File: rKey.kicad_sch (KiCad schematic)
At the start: 38 parts, among them IC1 BDX34C, J1 Conn_01x06, Q1 BC337, Q2 BC337, Q3 BC337, Q4 BC337, Q5 BC327, Q8 BC337, U1 TL084BCN, U2 LM7810_TO220

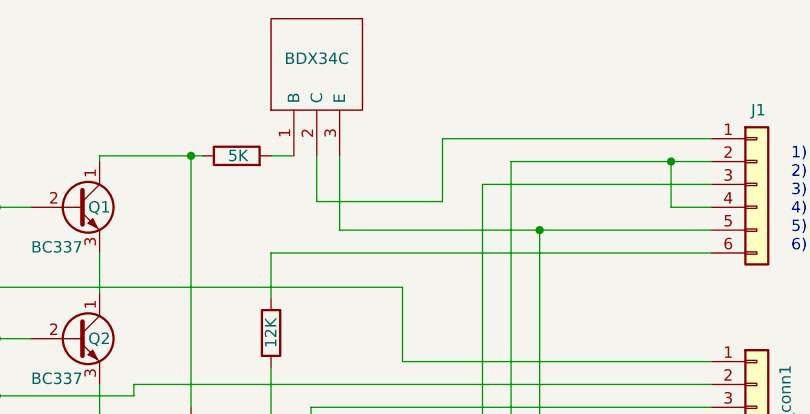
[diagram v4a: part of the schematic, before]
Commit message: Fix: floating tranistor's base
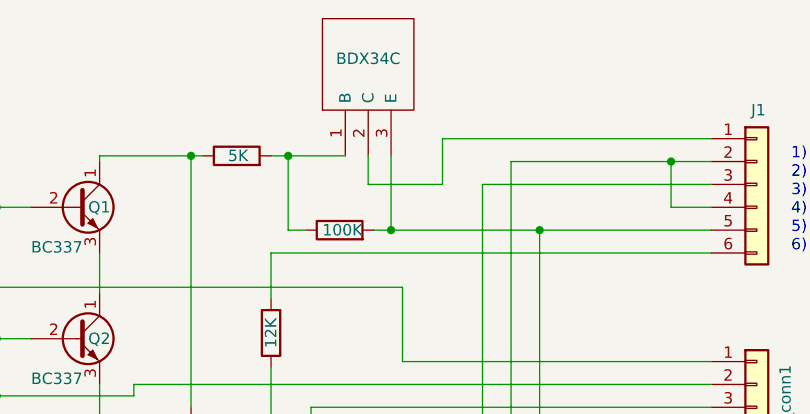
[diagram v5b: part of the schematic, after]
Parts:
- added R11: 100K, Resistor_THT:R_Axial_DIN0207_L6.3mm_D2.5mm_P10.16mm_Horizontal, symbol Device:R
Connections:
- net at IC1.1 (B), R10.2: now also R11.1
- net at IC1.3 (E), J1.5 (Pin_5), R6.2: now also R11.2
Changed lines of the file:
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@@
   (junction (at 200.025 86.36) (diameter 0) (color 0 0 0 0)
   )
+  (junction (at 201.93 53.34) (diameter 0) (color 0 0 0 0)
+  )
   (junction (at 76.2 92.71) (diameter 0) (color 0 0 0 0)
   )
@@
   )
   (junction (at 77.47 76.835) (diameter 0) (color 0 0 0 0)
+  )
+  (junction (at 213.36 61.595) (diameter 0) (color 0 0 0 0)
   )
   (junction (at 59.055 116.205) (diameter 0) (color 0 0 0 0)
@@
     (stroke (width 0) (type default) (color 0 0 0 0))
   )
+  (wire (pts (xy 201.93 61.595) (xy 201.93 53.34))
+    (stroke (width 0) (type default) (color 0 0 0 0))
+  )
   (wire (pts (xy 204.47 81.28) (xy 248.92 81.28))
     (stroke (width 0) (type default) (color 0 0 0 0))
@@
     (stroke (width 0) (type default) (color 0 0 0 0))
   )
-  (wire (pts (xy 219.075 58.42) (xy 219.075 51.435))
+  (wire (pts (xy 219.075 56.515) (xy 219.075 51.435))
     (stroke (width 0) (type default) (color 0 0 0 0))
   )
@@
     (stroke (width 0) (type default) (color 0 0 0 0))
   )
+  (wire (pts (xy 200.025 53.34) (xy 201.93 53.34))
+    (stroke (width 0) (type default) (color 0 0 0 0))
+  )
   (wire (pts (xy 149.86 59.055) (xy 157.48 59.055))
     (stroke (width 0) (type default) (color 0 0 0 0))
@@
     (stroke (width 0) (type default) (color 0 0 0 0))
   )
+  (wire (pts (xy 211.455 61.595) (xy 213.36 61.595))
+    (stroke (width 0) (type default) (color 0 0 0 0))
+  )
   (wire (pts (xy 138.43 87.63) (xy 138.43 95.25))
     (stroke (width 0) (type default) (color 0 0 0 0))
@@
     (stroke (width 0) (type default) (color 0 0 0 0))
   )
-  (wire (pts (xy 207.645 61.595) (xy 229.87 61.595))
+  (wire (pts (xy 213.36 61.595) (xy 229.87 61.595))
     (stroke (width 0) (type default) (color 0 0 0 0))
   )
@@
     (stroke (width 0) (type default) (color 0 0 0 0))
   )
-  (wire (pts (xy 205.105 53.34) (xy 205.105 58.42))
+  (wire (pts (xy 210.82 53.34) (xy 210.82 56.515))
     (stroke (width 0) (type default) (color 0 0 0 0))
   )
@@
     (stroke (width 0) (type default) (color 0 0 0 0))
   )
-  (wire (pts (xy 200.025 53.34) (xy 202.565 53.34))
-    (stroke (width 0) (type default) (color 0 0 0 0))
-  )
   (wire (pts (xy 167.64 100.965) (xy 167.64 95.25))
     (stroke (width 0) (type default) (color 0 0 0 0))
@@
     (stroke (width 0) (type default) (color 0 0 0 0))
   )
-  (wire (pts (xy 207.645 61.595) (xy 207.645 53.34))
+  (wire (pts (xy 213.36 61.595) (xy 213.36 53.34))
     (stroke (width 0) (type default) (color 0 0 0 0))
   )
@@
     (stroke (width 0) (type default) (color 0 0 0 0))
   )
-  (wire (pts (xy 205.105 58.42) (xy 219.075 58.42))
+  (wire (pts (xy 210.82 56.515) (xy 219.075 56.515))
     (stroke (width 0) (type default) (color 0 0 0 0))
   )
@@
     (stroke (width 0) (type default) (color 0 0 0 0))
   )
+  (wire (pts (xy 203.835 61.595) (xy 201.93 61.595))
+    (stroke (width 0) (type default) (color 0 0 0 0))
+  )
   (wire (pts (xy 47.625 81.28) (xy 47.625 76.2))
     (stroke (width 0) (type default) (color 0 0 0 0))
@@
   )
   (wire (pts (xy 89.535 95.25) (xy 93.98 95.25))
+    (stroke (width 0) (type default) (color 0 0 0 0))
+  )
+  (wire (pts (xy 201.93 53.34) (xy 208.28 53.34))
     (stroke (width 0) (type default) (color 0 0 0 0))
   )
@@
     (pin "2")
     (pin "3")
+  )
+  (symbol (lib_id "Device:R") (at 207.645 61.595 90) (unit 1)
+    (in_bom yes) (on_board yes)
+    (property "Reference" "R11" (id 0) (at 206.3749 59.055 0)
+      (effects (font (size 1.27 1.27)) (justify left) hide)
+    )
+    (property "Value" "100K" (id 1) (at 210.185 61.595 90)
+      (effects (font (size 1.27 1.27)) (justify left))
+    )
+    (property "Footprint" "Resistor_THT:R_Axial_DIN0207_L6.3mm_D2.5mm_P10.16mm_Horizontal" (id 2) (at 207.645 63.373 90)
+      (effects (font (size 1.27 1.27)) hide)
+    )
+    (property "Datasheet" "~" (id 3) (at 207.645 61.595 0)
+      (effects (font (size 1.27 1.27)) hide)
+    )
+    (pin "1")
+    (pin "2")
   )
   (symbol (lib_id "Device:R_Potentiometer_Small") (at 71.755 80.645 0) (unit 1)
@@
     (pin "6")
   )
-  (symbol (lib_id "BDX34C:BDX34C") (at 202.565 53.34 90) (unit 1)
-    (in_bom yes) (on_board yes)
-    (property "Reference" "IC1" (id 0) (at 215.9 43.18 0)
-      (effects (font (size 1.27 1.27)) hide)
-    )
-    (property "Value" "BDX34C" (id 1) (at 205.105 42.545 90))
-    (property "Footprint" "BDX34C:TO270P460X1020X2008-3P" (id 2) (at 200.025 36.83 0)
-      (effects (font (size 1.27 1.27)) (justify left) hide)
-    )
-    (property "Datasheet" "http://www.st.com/web/en/resource/technical/document/datasheet/CD00000901.pdf" (id 3) (at 202.565 36.83 0)
-      (effects (font (size 1.27 1.27)) (justify left) hide)
-    )
-    (property "Description" "BDX34C, Darlington Transistor, PNP 10 A 100 V HFE:750, 3-Pin, TO-220" (id 4) (at 205.105 36.83 0)
-      (effects (font (size 1.27 1.27)) (justify left) hide)
-    )
-    (property "Height" "4.6" (id 5) (at 207.645 36.83 0)
-      (effects (font (size 1.27 1.27)) (justify left) hide)
-    )
-    (property "Manufacturer_Name" "STMicroelectronics" (id 6) (at 210.185 36.83 0)
-      (effects (font (size 1.27 1.27)) (justify left) hide)
-    )
-    (property "Manufacturer_Part_Number" "BDX34C" (id 7) (at 212.725 36.83 0)
-      (effects (font (size 1.27 1.27)) (justify left) hide)
-    )
-    (property "Mouser Part Number" "511-BDX34C" (id 8) (at 215.265 36.83 0)
-      (effects (font (size 1.27 1.27)) (justify left) hide)
-    )
-    (property "Mouser Price/Stock" "https://www.mouser.co.uk/ProductDetail/STMicroelectronics/BDX34C?qs=vrHyyfhkd3JVtBIF%2FbOetQ%3D%3D" (id 9) (at 217.805 36.83 0)
-      (effects (font (size 1.27 1.27)) (justify left) hide)
-    )
-    (property "Arrow Part Number" "BDX34C" (id 10) (at 220.345 36.83 0)
-      (effects (font (size 1.27 1.27)) (justify left) hide)
-    )
-    (property "Arrow Price/Stock" "https://www.arrow.com/en/products/bdx34c/stmicroelectronics" (id 11) (at 222.885 36.83 0)
-      (effects (font (size 1.27 1.27)) (justify left) hide)
-    )
-    (property "Mouser Testing Part Number" "" (id 12) (at 225.425 36.83 0)
-      (effects (font (size 1.27 1.27)) (justify left) hide)
-    )
-    (property "Mouser Testing Price/Stock" "" (id 13) (at 227.965 36.83 0)
+  (symbol (lib_id "BDX34C:BDX34C") (at 208.28 53.34 90) (unit 1)
+    (in_bom yes) (on_board yes)
+    (property "Reference" "IC1" (id 0) (at 221.615 43.18 0)
+      (effects (font (size 1.27 1.27)) hide)
+    )
+    (property "Value" "BDX34C" (id 1) (at 210.82 42.545 90))
+    (property "Footprint" "BDX34C:TO270P460X1020X2008-3P" (id 2) (at 205.74 36.83 0)
+      (effects (font (size 1.27 1.27)) (justify left) hide)
+    )
+    (property "Datasheet" "http://www.st.com/web/en/resource/technical/document/datasheet/CD00000901.pdf" (id 3) (at 208.28 36.83 0)
+      (effects (font (size 1.27 1.27)) (justify left) hide)
+    )
+    (property "Description" "BDX34C, Darlington Transistor, PNP 10 A 100 V HFE:750, 3-Pin, TO-220" (id 4) (at 210.82 36.83 0)
+      (effects (font (size 1.27 1.27)) (justify left) hide)
+    )
+    (property "Height" "4.6" (id 5) (at 213.36 36.83 0)
+      (effects (font (size 1.27 1.27)) (justify left) hide)
+    )
+    (property "Manufacturer_Name" "STMicroelectronics" (id 6) (at 215.9 36.83 0)
+      (effects (font (size 1.27 1.27)) (justify left) hide)
+    )
+    (property "Manufacturer_Part_Number" "BDX34C" (id 7) (at 218.44 36.83 0)
+      (effects (font (size 1.27 1.27)) (justify left) hide)
+    )
+    (property "Mouser Part Number" "511-BDX34C" (id 8) (at 220.98 36.83 0)
+      (effects (font (size 1.27 1.27)) (justify left) hide)
+    )
+    (property "Mouser Price/Stock" "https://www.mouser.co.uk/ProductDetail/STMicroelectronics/BDX34C?qs=vrHyyfhkd3JVtBIF%2FbOetQ%3D%3D" (id 9) (at 223.52 36.83 0)
+      (effects (font (size 1.27 1.27)) (justify left) hide)
+    )
+    (property "Arrow Part Number" "BDX34C" (id 10) (at 226.06 36.83 0)
+      (effects (font (size 1.27 1.27)) (justify left) hide)
+    )
+    (property "Arrow Price/Stock" "https://www.arrow.com/en/products/bdx34c/stmicroelectronics" (id 11) (at 228.6 36.83 0)
+      (effects (font (size 1.27 1.27)) (justify left) hide)
+    )
+    (property "Mouser Testing Part Number" "" (id 12) (at 231.14 36.83 0)
+      (effects (font (size 1.27 1.27)) (justify left) hide)
+    )
+    (property "Mouser Testing Price/Stock" "" (id 13) (at 233.68 36.83 0)
       (effects (font (size 1.27 1.27)) (justify left) hide)
     )
@@
       (reference "R10") (unit 1) (value "5K") (footprint "Resistor_THT:R_Axial_DIN0207_L6.3mm_D2.5mm_P10.16mm_Horizontal")
     )
+    (path "/14746be3-d3bc-4979-bae8-482bd75b4106"
+      (reference "R11") (unit 1) (value "100K") (footprint "Resistor_THT:R_Axial_DIN0207_L6.3mm_D2.5mm_P10.16mm_Horizontal")
+    )
     (path "/948aca6f-8f62-4a55-90cb-26e4af45dc7f"

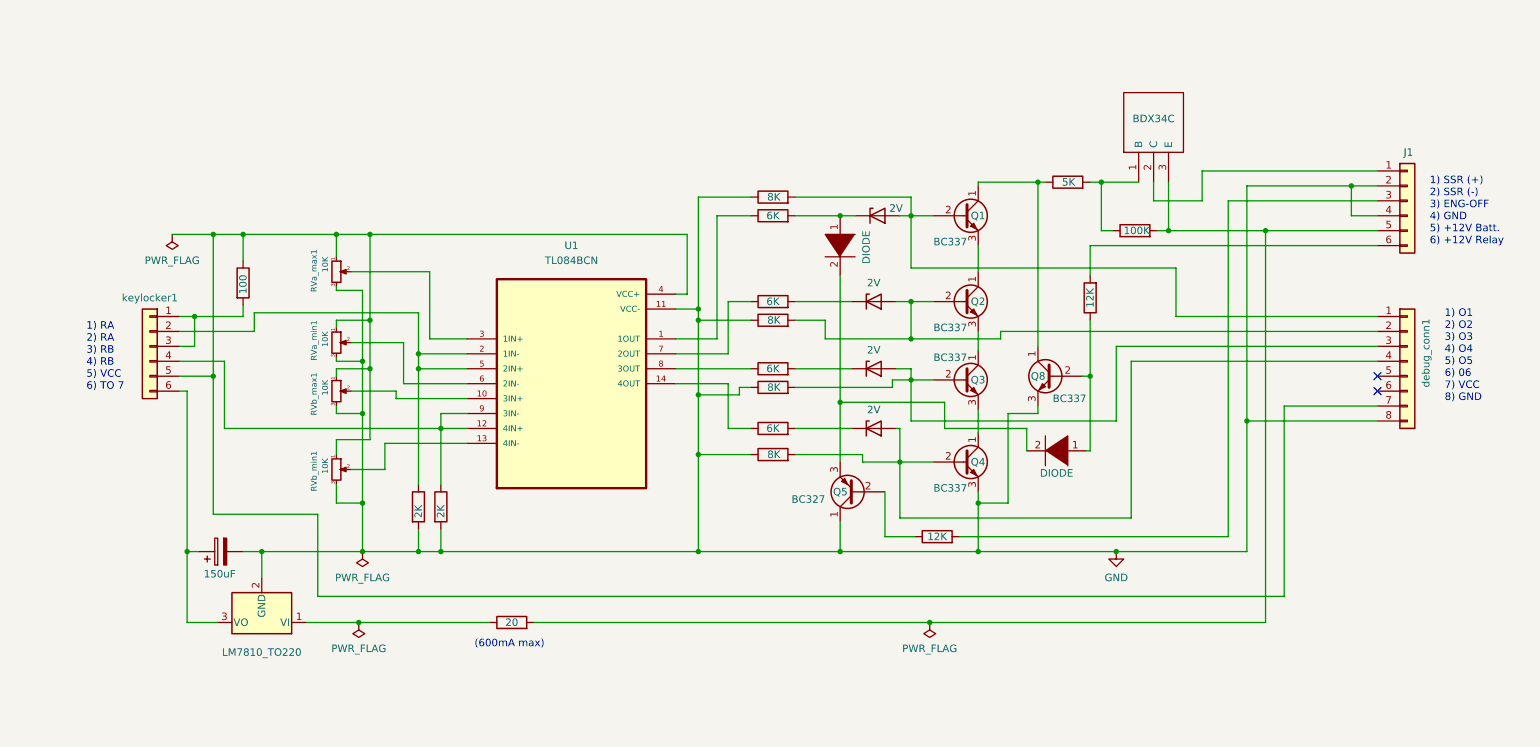
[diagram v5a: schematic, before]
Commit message: Fix: unuseful (diodes) components removed
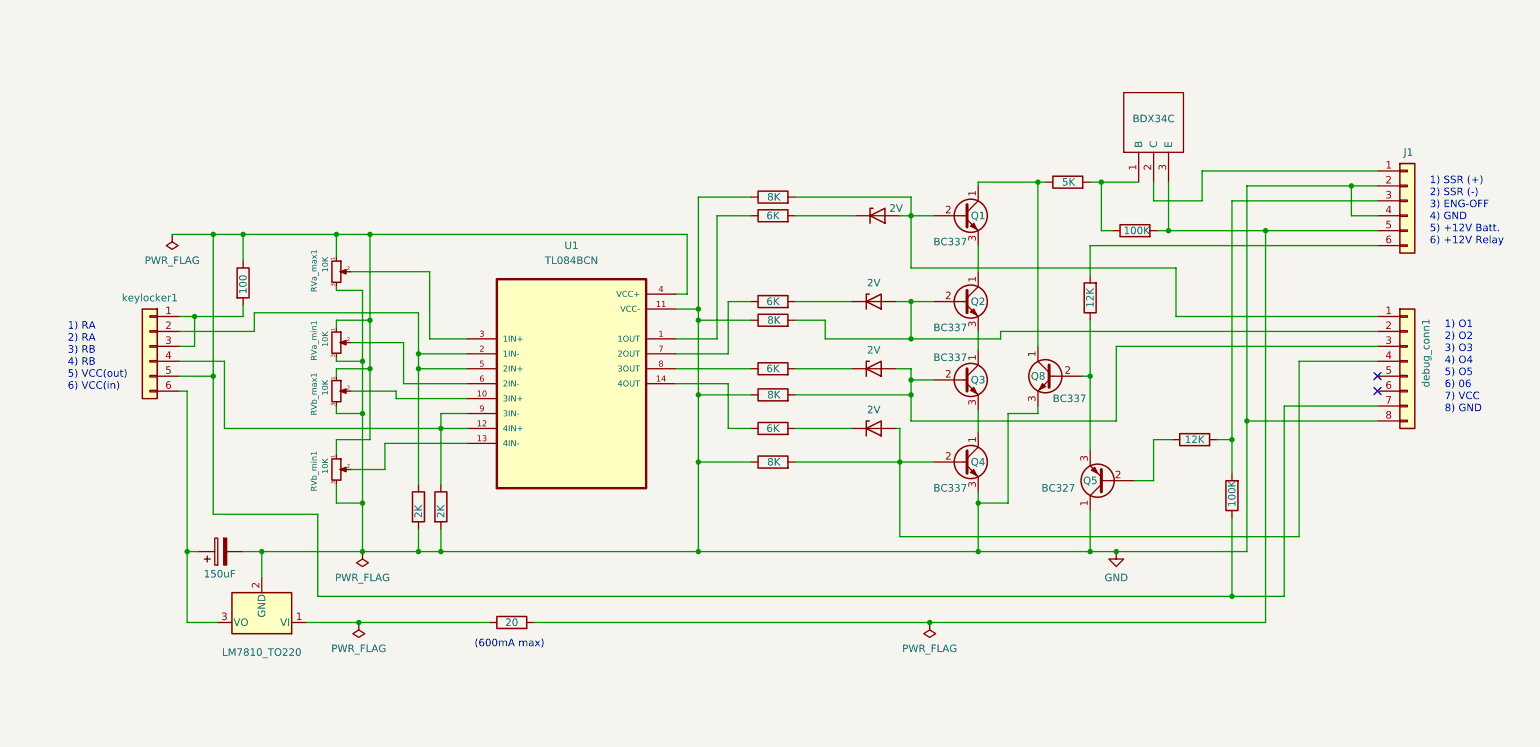
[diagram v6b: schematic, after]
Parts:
- removed D1, D6: DIODE, Diode_THT:D_DO-34_SOD68_P10.16mm_Horizontal, symbol pspice:DIODE
- added R14: 100K, Resistor_THT:R_Axial_DIN0207_L6.3mm_D2.5mm_P10.16mm_Horizontal, symbol Device:R
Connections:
- net at J1.3 (Pin_3), R13.2: now also R14.2
- net at Q5.3 (E): now also Q8.2 (B), R9.1
- net at R1.1, RVa_max1.1, RVa_min1.1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: now also R14.1
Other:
- note added: "1) RA 2) RA 3) RB 4) RB 5) VCC(out) 6) VCC(in)"
- note removed: "1) RA 2) RA 3) RB 4) RB 5) VCC 6) TO 7"
- moved on the sheet: Q5

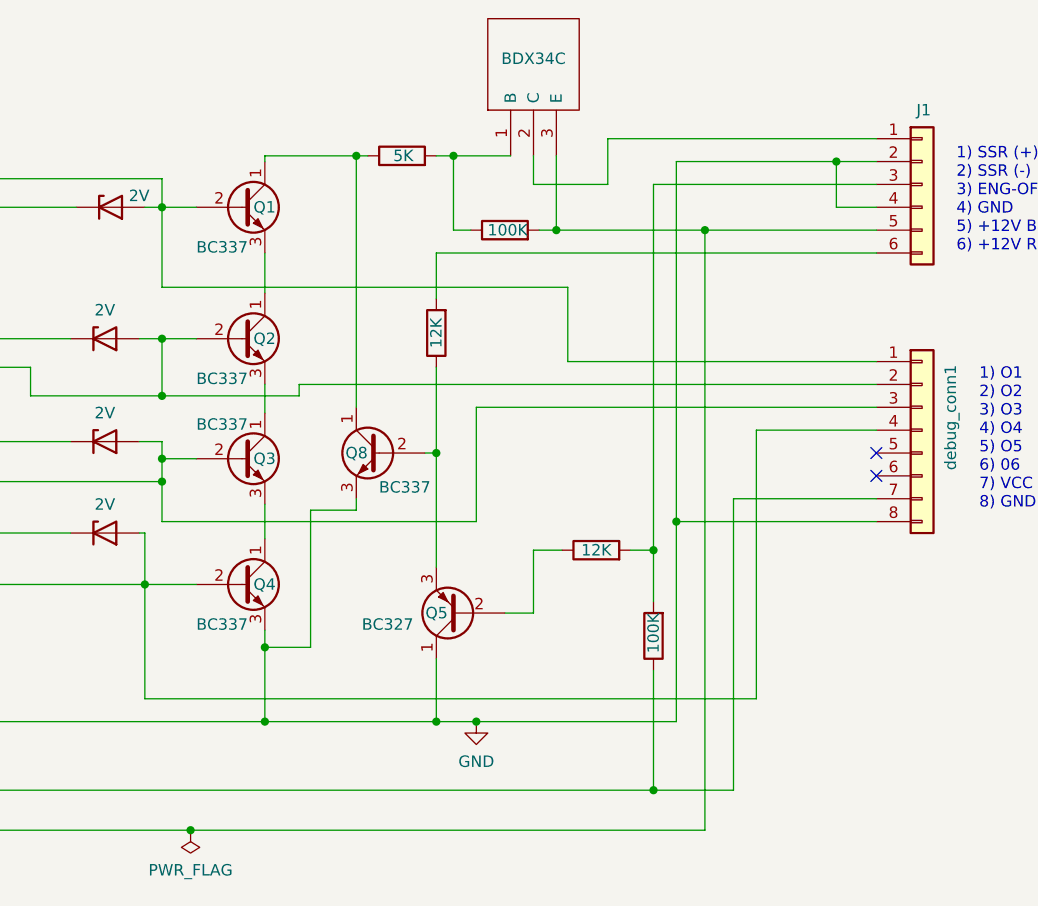
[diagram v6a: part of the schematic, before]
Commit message: Fix: Zenner diode added
To allow the STOP button to turn off the services' controller, the Zenner has been placed between the ON status holdon pin
and its BC327 transistor. When you stop the engine your key must be not plugged, obviosely.
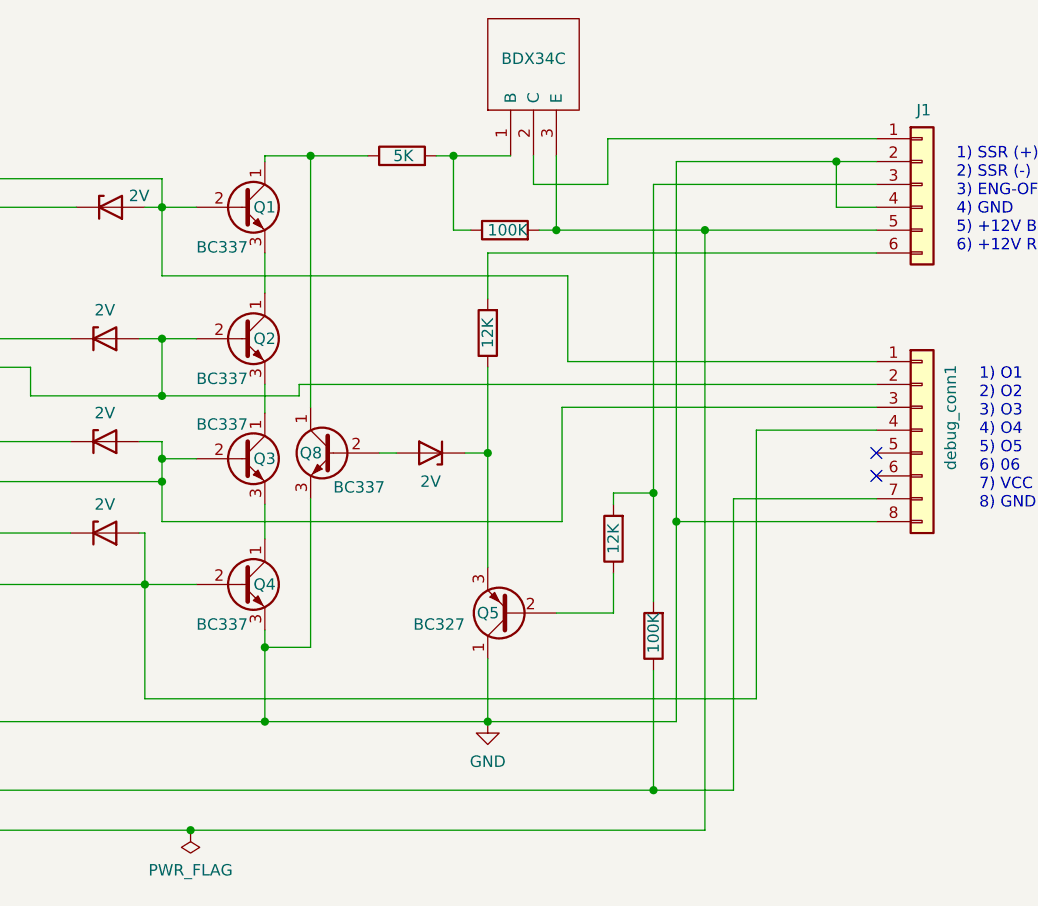
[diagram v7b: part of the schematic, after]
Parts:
- added ZD1: 2V, Diode_THT:D_DO-34_SOD68_P10.16mm_Horizontal, symbol Device:D_Zener
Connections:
- net at Q5.3 (E), R9.1: now also ZD1.1 (K); no longer Q8.2 (B)
- new net: Q8.2 (B), ZD1.2 (A)
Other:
- moved on the sheet: Q5, Q8
